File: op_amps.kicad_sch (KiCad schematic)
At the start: 44 parts, among them U10 ${SIM.PARAMS}, U11 ${SIM.PARAMS}, U12 ${SIM.PARAMS}, U13 ${SIM.PARAMS}, U14 ${SIM.PARAMS}, U15 ${SIM.PARAMS}, U16 ${SIM.PARAMS}, U17 ${SIM.PARAMS}, U18 ${SIM.PARAMS}, U19 ${SIM.PARAMS}, U20 ${SIM.PARAMS}, U21 ${SIM.PARAMS}, U22 ${SIM.PARAMS}, U23 ${SIM.PARAMS}, U8 ${SIM.PARAMS}, U9 ${SIM.PARAMS}

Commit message: Before 10K resistors change
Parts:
- R15, R16, R17, R18, R19, R20, R21, R22, R23, R24, R25, R26, R27, R28, R29, R30, R31, R32, R33, R34, R44, R45, R46, R47: footprint (none) -> Resistor_SMD:R_1206_3216Metric_Pad1.30x1.75mm_HandSolder
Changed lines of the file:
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@@
 			)
 		)
-		(property "Footprint" ""
+		(property "Footprint" "Resistor_SMD:R_1206_3216Metric_Pad1.30x1.75mm_HandSolder"
 			(at 120.65 79.248 90)
 			(effects
@@
 			)
 		)
-		(property "Footprint" ""
+		(property "Footprint" "Resistor_SMD:R_1206_3216Metric_Pad1.30x1.75mm_HandSolder"
 			(at 120.65 174.498 90)
 			(effects
@@
 			)
 		)
-		(property "Footprint" ""
+		(property "Footprint" "Resistor_SMD:R_1206_3216Metric_Pad1.30x1.75mm_HandSolder"
 			(at 106.68 197.358 90)
 			(effects
@@
 			)
 		)
-		(property "Footprint" ""
+		(property "Footprint" "Resistor_SMD:R_1206_3216Metric_Pad1.30x1.75mm_HandSolder"
 			(at 96.012 152.4 90)
 			(effects
@@
 			)
 		)
-		(property "Footprint" ""
+		(property "Footprint" "Resistor_SMD:R_1206_3216Metric_Pad1.30x1.75mm_HandSolder"
 			(at 83.82 119.888 90)
 			(effects
@@
 			)
 		)
-		(property "Footprint" ""
+		(property "Footprint" "Resistor_SMD:R_1206_3216Metric_Pad1.30x1.75mm_HandSolder"
 			(at 106.68 102.108 90)
 			(effects
@@
 			)
 		)
-		(property "Footprint" ""
+		(property "Footprint" "Resistor_SMD:R_1206_3216Metric_Pad1.30x1.75mm_HandSolder"
 			(at 106.68 55.118 90)
 			(effects
@@
 			)
 		)
-		(property "Footprint" ""
+		(property "Footprint" "Resistor_SMD:R_1206_3216Metric_Pad1.30x1.75mm_HandSolder"
 			(at 83.82 72.898 90)
 			(effects
@@
 			)
 		)
-		(property "Footprint" ""
+		(property "Footprint" "Resistor_SMD:R_1206_3216Metric_Pad1.30x1.75mm_HandSolder"
 			(at 58.42 168.148 90)
 			(effects
@@
 			)
 		)
-		(property "Footprint" ""
+		(property "Footprint" "Resistor_SMD:R_1206_3216Metric_Pad1.30x1.75mm_HandSolder"
 			(at 83.82 168.148 90)
 			(effects
@@
 			)
 		)
-		(property "Footprint" ""
+		(property "Footprint" "Resistor_SMD:R_1206_3216Metric_Pad1.30x1.75mm_HandSolder"
 			(at 58.42 215.138 90)
 			(effects
@@
 			)
 		)
-		(property "Footprint" ""
+		(property "Footprint" "Resistor_SMD:R_1206_3216Metric_Pad1.30x1.75mm_HandSolder"
 			(at 106.68 150.368 90)
 			(effects
@@
 			)
 		)
-		(property "Footprint" ""
+		(property "Footprint" "Resistor_SMD:R_1206_3216Metric_Pad1.30x1.75mm_HandSolder"
 			(at 73.152 121.92 90)
 			(effects
@@
 			)
 		)
-		(property "Footprint" ""
+		(property "Footprint" "Resistor_SMD:R_1206_3216Metric_Pad1.30x1.75mm_HandSolder"
 			(at 96.012 57.15 90)
 			(effects
@@
 			)
 		)
-		(property "Footprint" ""
+		(property "Footprint" "Resistor_SMD:R_1206_3216Metric_Pad1.30x1.75mm_HandSolder"
 			(at 58.42 72.898 90)
 			(effects
@@
 			)
 		)
-		(property "Footprint" ""
+		(property "Footprint" "Resistor_SMD:R_1206_3216Metric_Pad1.30x1.75mm_HandSolder"
 			(at 83.82 215.138 90)
 			(effects
@@
 			)
 		)
-		(property "Footprint" ""
+		(property "Footprint" "Resistor_SMD:R_1206_3216Metric_Pad1.30x1.75mm_HandSolder"
 			(at 73.152 74.93 90)
 			(effects
@@
 			)
 		)
-		(property "Footprint" ""
+		(property "Footprint" "Resistor_SMD:R_1206_3216Metric_Pad1.30x1.75mm_HandSolder"
 			(at 120.65 126.238 90)
 			(effects
@@
 			)
 		)
-		(property "Footprint" ""
+		(property "Footprint" "Resistor_SMD:R_1206_3216Metric_Pad1.30x1.75mm_HandSolder"
 			(at 120.65 221.488 90)
 			(effects
@@
 			)
 		)
-		(property "Footprint" ""
+		(property "Footprint" "Resistor_SMD:R_1206_3216Metric_Pad1.30x1.75mm_HandSolder"
 			(at 58.42 119.888 90)
 			(effects
@@
 			)
 		)
-		(property "Footprint" ""
+		(property "Footprint" "Resistor_SMD:R_1206_3216Metric_Pad1.30x1.75mm_HandSolder"
 			(at 73.152 217.17 90)
 			(effects
@@
 			)
 		)
-		(property "Footprint" ""
+		(property "Footprint" "Resistor_SMD:R_1206_3216Metric_Pad1.30x1.75mm_HandSolder"
 			(at 73.152 170.18 90)
 			(effects
@@
 			)
 		)
-		(property "Footprint" ""
+		(property "Footprint" "Resistor_SMD:R_1206_3216Metric_Pad1.30x1.75mm_HandSolder"
 			(at 96.012 104.14 90)
 			(effects
@@
 			)
 		)
-		(property "Footprint" ""
+		(property "Footprint" "Resistor_SMD:R_1206_3216Metric_Pad1.30x1.75mm_HandSolder"
 			(at 96.012 199.39 90)
 			(effects

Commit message: Before capcitor update
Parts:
- R15, R16, R17, R18, R19, R20, R21, R22, R23, R24, R25, R26, R27, R28, R29, R30, R31, R32, R33, R34: value R -> 10k
- R44, R45, R46, R47: value R -> 10M
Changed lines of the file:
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@@
 			)
 		)
-		(property "Value" "R"
+		(property "Value" "10M"
 			(at 118.618 80.772 90)
 			(effects
@@
 		(dnp no)
 		(property "Reference" "R46"
-			(at 121.92 176.022 90)
+			(at 122.936 176.276 90)
 			(effects
 				(font
@@
 			)
 		)
-		(property "Value" "R"
+		(property "Value" "10M"
 			(at 118.618 176.022 90)
 			(effects
@@
 			)
 		)
-		(property "Value" "R"
+		(property "Value" "10k"
 			(at 106.68 191.77 90)
 			(effects
@@
 			)
 		)
-		(property "Value" "R"
+		(property "Value" "10k"
 			(at 100.33 153.6699 0)
 			(effects
@@
 			)
 		)
-		(property "Value" "R"
-			(at 82.296 120.65 90)
+		(property "Value" "10k"
+			(at 84.836 122.682 90)
 			(effects
 				(font
@@
 			)
 		)
-		(property "Value" "R"
+		(property "Value" "10k"
 			(at 106.68 96.52 90)
 			(effects
@@
 			)
 		)
-		(property "Value" "R"
+		(property "Value" "10k"
 			(at 106.68 49.53 90)
 			(effects
@@
 			)
 		)
-		(property "Value" "R"
+		(property "Value" "10k"
 			(at 82.296 73.66 90)
 			(effects
@@
 			)
 		)
-		(property "Value" "R"
+		(property "Value" "10k"
 			(at 56.896 168.91 90)
 			(effects
@@
 			)
 		)
-		(property "Value" "R"
+		(property "Value" "10k"
 			(at 82.296 168.91 90)
 			(effects
@@
 			)
 		)
-		(property "Value" "R"
+		(property "Value" "10k"
 			(at 56.896 215.9 90)
 			(effects
@@
 			)
 		)
-		(property "Value" "R"
+		(property "Value" "10k"
 			(at 106.68 144.78 90)
 			(effects
@@
 			)
 		)
-		(property "Value" "R"
+		(property "Value" "10k"
 			(at 77.47 123.1899 0)
 			(effects
@@
 			)
 		)
-		(property "Value" "R"
+		(property "Value" "10k"
 			(at 100.33 58.4199 0)
 			(effects
@@
 			)
 		)
-		(property "Value" "R"
+		(property "Value" "10k"
 			(at 56.896 73.66 90)
 			(effects
@@
 			)
 		)
-		(property "Value" "R"
+		(property "Value" "10k"
 			(at 82.296 215.9 90)
 			(effects
@@
 			)
 		)
-		(property "Value" "R"
+		(property "Value" "10k"
 			(at 77.47 76.1999 0)
 			(effects
@@
 		(dnp no)
 		(property "Reference" "R45"
-			(at 121.92 127.762 90)
+			(at 122.936 127.762 90)
 			(effects
 				(font
@@
 			)
 		)
-		(property "Value" "R"
+		(property "Value" "10M"
 			(at 118.618 127.762 90)
 			(effects
@@
 		(dnp no)
 		(property "Reference" "R47"
-			(at 121.92 223.012 90)
+			(at 122.428 223.012 90)
 			(effects
 				(font
@@
 			)
 		)
-		(property "Value" "R"
+		(property "Value" "10M"
 			(at 118.618 223.012 90)
 			(effects
@@
 			)
 		)
-		(property "Value" "R"
+		(property "Value" "10k"
 			(at 56.896 120.65 90)
 			(effects
@@
 			)
 		)
-		(property "Value" "R"
+		(property "Value" "10k"
 			(at 77.47 218.4399 0)
 			(effects
@@
 			)
 		)
-		(property "Value" "R"
+		(property "Value" "10k"
 			(at 77.47 171.4499 0)
 			(effects
@@
 			)
 		)
-		(property "Value" "R"
+		(property "Value" "10k"
 			(at 100.33 105.4099 0)
 			(effects
@@
 			)
 		)
-		(property "Value" "R"
+		(property "Value" "10k"
 			(at 100.33 200.6599 0)
 			(effects

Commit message: updated capacitor values
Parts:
- C1, C2, C3, C4: value C -> 100nF
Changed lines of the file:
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@@
 			)
 		)
-		(property "Value" "C"
+		(property "Value" "100nF"
 			(at 120.65 161.29 90)
 			(effects
@@
 			)
 		)
-		(property "Value" "C"
+		(property "Value" "100nF"
 			(at 120.65 66.04 90)
 			(effects
@@
 			)
 		)
-		(property "Value" "C"
+		(property "Value" "100nF"
 			(at 120.65 208.28 90)
 			(effects
@@
 			)
 		)
-		(property "Value" "C"
+		(property "Value" "100nF"
 			(at 120.65 113.03 90)
 			(effects

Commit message: Updated: power
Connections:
- net -VCC is gone; now on net GND: U10.4 (V-), U11.4 (V-), U12.4 (V-), U13.4 (V-), U14.4 (V-), U15.4 (V-), U16.4 (V-), U17.4 (V-), U18.4 (V-), U19.4 (V-), U20.4 (V-), U21.4 (V-), U22.4 (V-), U23.4 (V-), U8.4 (V-), U9.4 (V-)

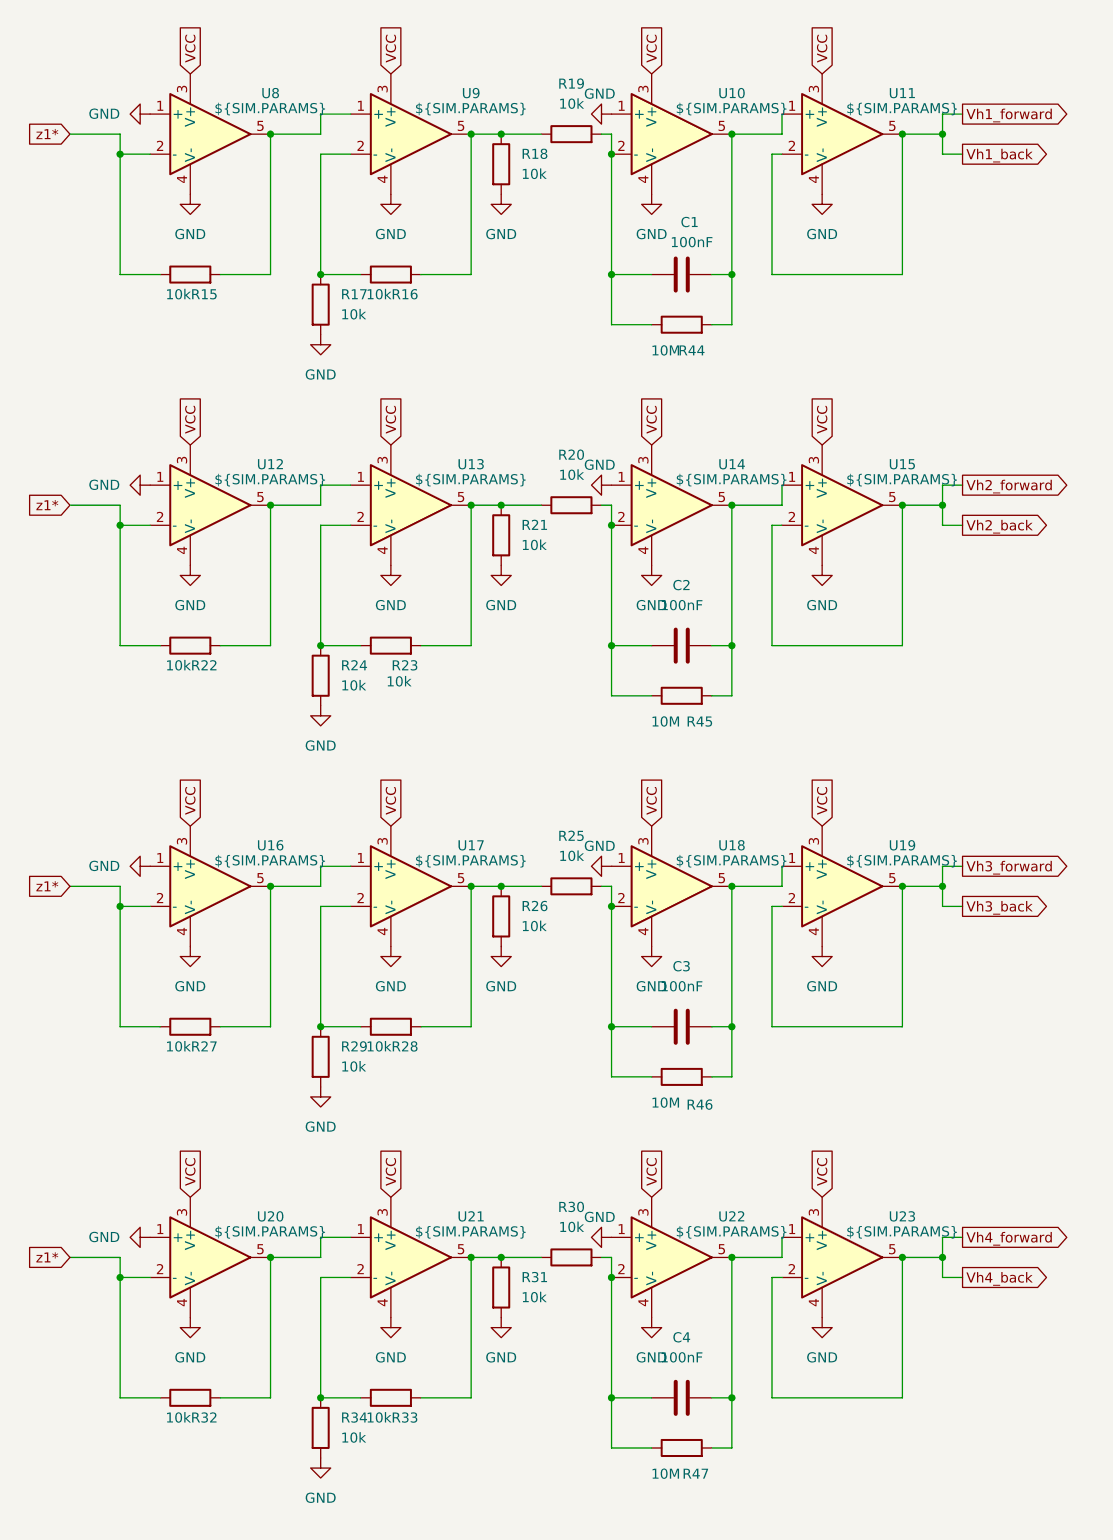
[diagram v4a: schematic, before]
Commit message: Updated: op amps
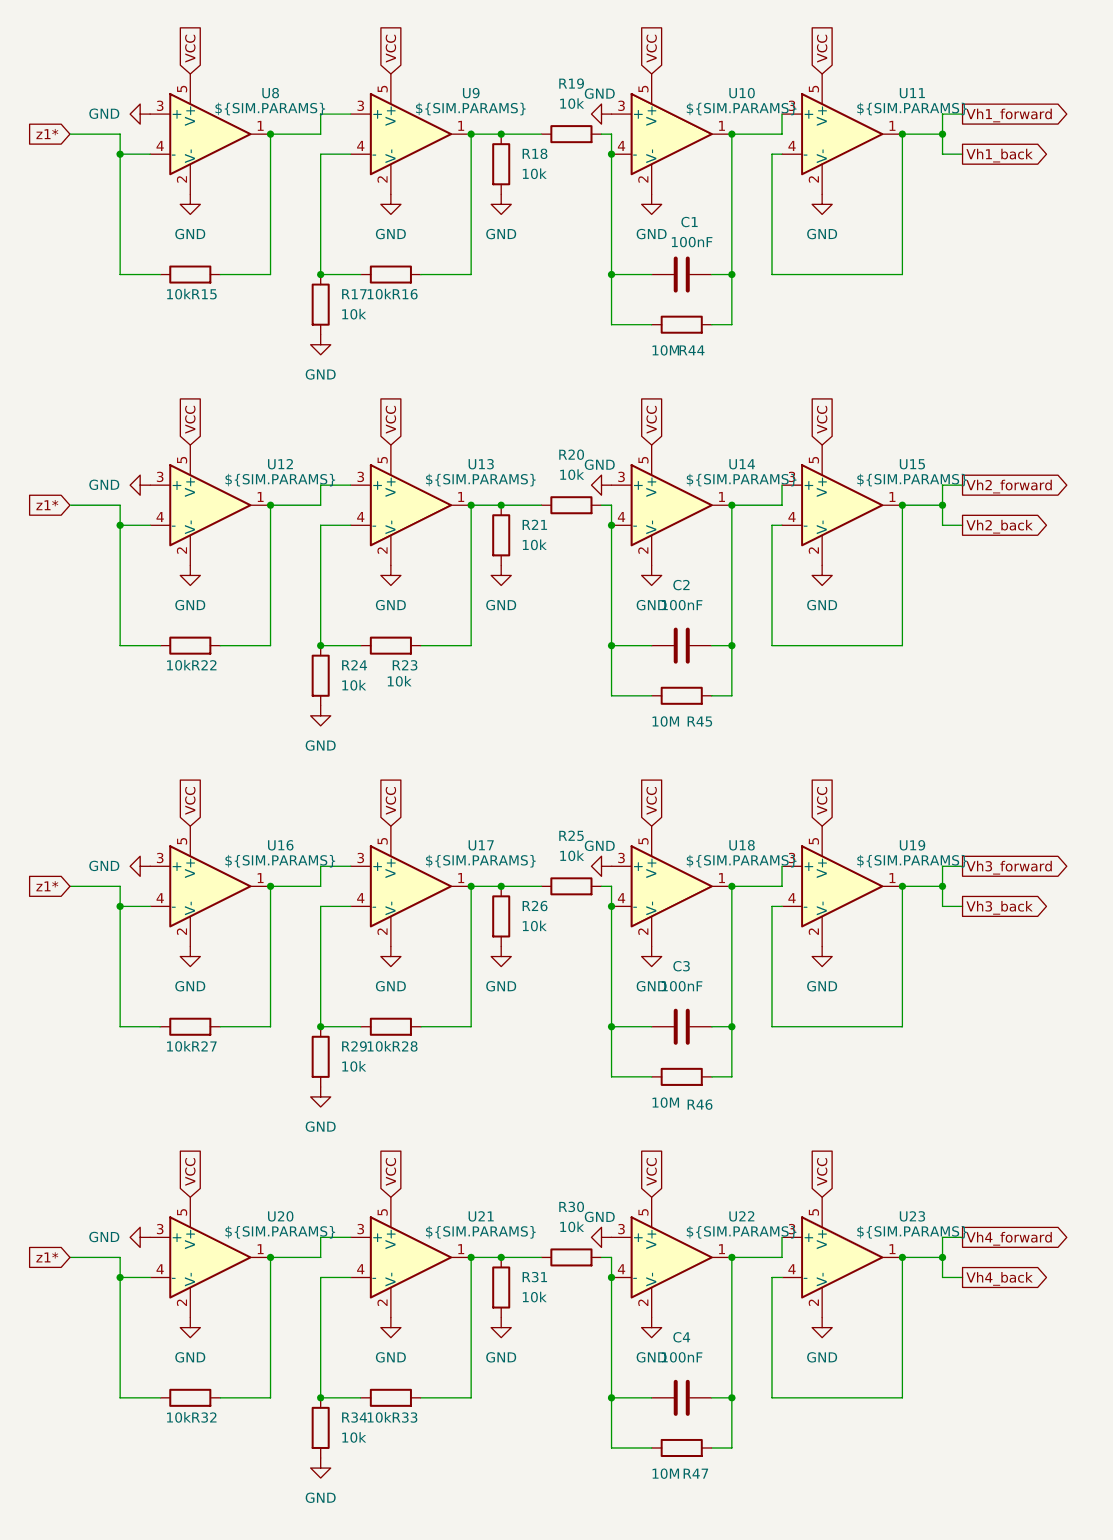
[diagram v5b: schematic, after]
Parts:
- C1, C2, C3, C4: footprint (none) -> Capacitor_SMD:C_1206_3216Metric_Pad1.33x1.80mm_HandSolder
- U10, U11, U12, U13, U14, U15, U16, U17, U18, U19, U20, U21, U22, U23, U8, U9: footprint (none) -> Package_TO_SOT_SMD:SOT-23-5; symbol Simulation_SPICE:OPAMP -> Amplifier_Operational:TLV9061xDBV
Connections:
- net GND: now also U10.2 (V-), U10.3 (+), U11.2 (V-), U12.2 (V-), U12.3 (+), U13.2 (V-), U14.2 (V-), U14.3 (+), U15.2 (V-), U16.2 (V-), U16.3 (+), U17.2 (V-), U18.2 (V-), U18.3 (+), U19.2 (V-), U20.2 (V-), U20.3 (+), U21.2 (V-), U22.2 (V-), U22.3 (+), U23.2 (V-), U8.2 (V-), U8.3 (+), U9.2 (V-); no longer U10.1 (+), U10.4 (V-), U11.4 (V-), U12.1 (+), U12.4 (V-), U13.4 (V-), U14.1 (+), U14.4 (V-), U15.4 (V-), U16.1 (+), U16.4 (V-), U17.4 (V-), U18.1 (+), U18.4 (V-), U19.4 (V-), U20.1 (+), U20.4 (V-), U21.4 (V-), U22.1 (+), U22.4 (V-), U23.4 (V-), U8.1 (+), U8.4 (V-), U9.4 (V-)
- net VCC: now also U10.5 (V+), U11.5 (V+), U12.5 (V+), U13.5 (V+), U14.5 (V+), U15.5 (V+), U16.5 (V+), U17.5 (V+), U18.5 (V+), U19.5 (V+), U20.5 (V+), U21.5 (V+), U22.5 (V+), U23.5 (V+), U8.5 (V+), U9.5 (V+); no longer U10.3 (V+), U11.3 (V+), U12.3 (V+), U13.3 (V+), U14.3 (V+), U15.3 (V+), U16.3 (V+), U17.3 (V+), U18.3 (V+), U19.3 (V+), U20.3 (V+), U21.3 (V+), U22.3 (V+), U23.3 (V+), U8.3 (V+), U9.3 (V+)
- net Vh1_back: now also U11.1, U11.4 (-); no longer U11.2 (-), U11.5
- net Vh2_back: now also U15.1, U15.4 (-); no longer U15.2 (-), U15.5
- net Vh3_back: now also U19.1, U19.4 (-); no longer U19.2 (-), U19.5
- net Vh4_back: now also U23.1, U23.4 (-); no longer U23.2 (-), U23.5
- net z1*: now also U12.4 (-), U16.4 (-), U20.4 (-), U8.4 (-); no longer U12.2 (-), U16.2 (-), U20.2 (-), U8.2 (-)
- net at C1.1, R19.2, R44.1: now also U10.4 (-); no longer U10.2 (-)
- net at C1.2, R44.2: now also U10.1, U11.3 (+); no longer U10.5, U11.1 (+)
- net at C3.1, R25.2, R46.1: now also U18.4 (-); no longer U18.2 (-)
- net at C3.2, R46.2: now also U18.1, U19.3 (+); no longer U18.5, U19.1 (+)
- net at C4.2, R47.2: now also U22.1, U23.3 (+); no longer U22.5, U23.1 (+)
- net at R30.1, R31.1, R33.2: now also U21.1; no longer U21.5
- net at C4.1, R30.2, R47.1: now also U22.4 (-); no longer U22.2 (-)
- net at R23.1, R24.1: now also U13.4 (-); no longer U13.2 (-)
- net at R20.1, R21.1, R23.2: now also U13.1; no longer U13.5
- net at R25.1, R26.1, R28.2: now also U17.1; no longer U17.5
- net at C2.1, R20.2, R45.1: now also U14.4 (-); no longer U14.2 (-)
- net at R16.2, R18.1, R19.1: now also U9.1; no longer U9.5
- net at R16.1, R17.1: now also U9.4 (-); no longer U9.2 (-)
- net at C2.2, R45.2: now also U14.1, U15.3 (+); no longer U14.5, U15.1 (+)
- net at R28.1, R29.1: now also U17.4 (-); no longer U17.2 (-)
- net at R33.1, R34.1: now also U21.4 (-); no longer U21.2 (-)
- new net: R15.2, U8.1, U9.3 (+)
- new net: R22.2, U12.1, U13.3 (+)
- new net: R27.2, U16.1, U17.3 (+)
- new net: R32.2, U20.1, U21.3 (+)

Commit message: Updated: pots
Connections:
- net GND: no longer R17.2, R18.2, R21.2, R24.2, R26.2, R29.2, R31.2, R34.2, U10.3 (+), U12.3 (+), U14.3 (+), U16.3 (+), U18.3 (+), U20.3 (+), U22.3 (+), U8.3 (+)
- new net VREF: R17.2, R18.2, R21.2, R24.2, R26.2, R29.2, R31.2, R34.2, U10.3 (+), U12.3 (+), U14.3 (+), U16.3 (+), U18.3 (+), U20.3 (+), U22.3 (+), U8.3 (+)
